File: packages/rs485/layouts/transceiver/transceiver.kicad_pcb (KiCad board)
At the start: 2 copper layers, 3 parts

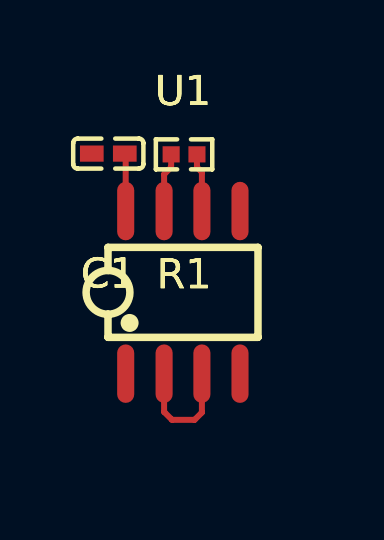
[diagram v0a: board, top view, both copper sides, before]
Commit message: Fix pulldown on RE pins
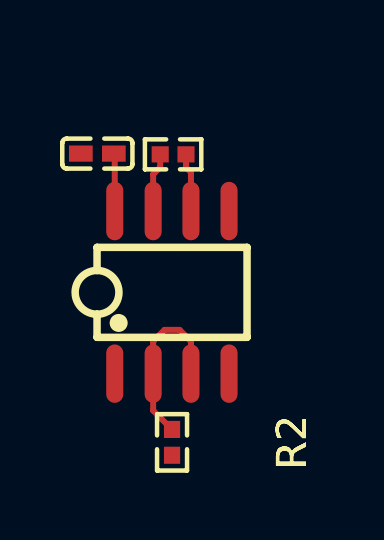
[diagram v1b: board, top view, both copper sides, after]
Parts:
- added R2: 10kΩ ±1% 62.5mW, atopile:R0402-56259e, F.Cu at (0.00, 5.00)
- moved R1 0.36 mm to (0.04, -4.60)
- moved U1 0.36 mm to (0.00, 0.00)
- moved C1 0.36 mm to (-2.49, -4.62)
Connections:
- R1 pad 1: line-1 -> line-4
- U1 pad 1: line-4 -> line
- U1 pad 2: line -> line-1
- U1 pad 3: line -> line-1
- U1 pad 6: line-1 -> line-4
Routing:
- net line: track 4.04 -> 0.00 mm
- net line-1: track 1.96 -> 5.86 mm
- net line-4: track 0.00 -> 1.96 mm

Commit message: Build all packages without designators on silkscreen.
Also disable fail_on_drc and enable keep_picked_parts for build
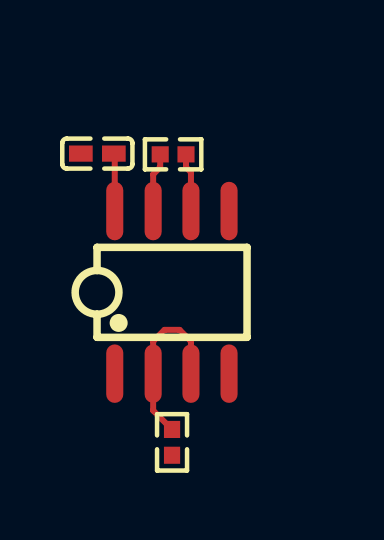
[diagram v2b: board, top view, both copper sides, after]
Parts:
- R1: value 121Ω ±1% 62.5mW -> 120Ω ±1% 62.5mW
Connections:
- R1 pad 1: line-4 -> line-2
- R1 pad 2: line-2 -> line-3
- R2 pad 1: line-1 -> line-4
- U1 pad 1: line -> line-1
- U1 pad 2: line-1 -> line-4
- U1 pad 3: line-1 -> line-4
- U1 pad 4: line-3 -> line
- U1 pad 6: line-4 -> line-2
- U1 pad 7: line-2 -> line-3
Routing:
- net line-1: track 5.86 -> 0.00 mm
- net line-4: track 1.96 -> 5.86 mm
- net line-3: track 0.00 -> 1.99 mm
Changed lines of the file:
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@@
     )
     (net 0 "")
-    (net 1 "line-2")
-    (net 2 "line")
-    (net 3 "line-3")
-    (net 4 "line-4")
+    (net 1 "line-3")
+    (net 2 "line-1")
+    (net 3 "line")
+    (net 4 "line-2")
     (net 5 "hv")
     (net 6 "gnd")
-    (net 7 "line-1")
+    (net 7 "line-4")
     (footprint "atopile:SOIC-8_L5.0-W4.0-P1.27-LS6.0-BL-294f77"
         (layer "F.Cu")
@@
             (size 0.57 1.95)
             (layers "F.Cu" "F.Mask" "F.Paste")
-            (net 2 "line")
+            (net 2 "line-1")
         )
         (pad "2" smd oval
@@
             (size 0.57 1.95)
             (layers "F.Cu" "F.Mask" "F.Paste")
-            (net 7 "line-1")
+            (net 7 "line-4")
         )
         (pad "3" smd oval
@@
             (size 0.57 1.95)
             (layers "F.Cu" "F.Mask" "F.Paste")
-            (net 7 "line-1")
+            (net 7 "line-4")
         )
         (pad "4" smd oval
@@
             (size 0.57 1.95)
             (layers "F.Cu" "F.Mask" "F.Paste")
-            (net 3 "line-3")
+            (net 3 "line")
         )
         (pad "5" smd oval
@@
             (size 0.57 1.95)
             (layers "F.Cu" "F.Mask" "F.Paste")
-            (net 4 "line-4")
+            (net 4 "line-2")
         )
         (pad "7" smd oval
@@
             (size 0.57 1.95)
             (layers "F.Cu" "F.Mask" "F.Paste")
-            (net 1 "line-2")
+            (net 1 "line-3")
         )
         (pad "8" smd oval
@@
             (at 0 -4 90)
             (layer "F.SilkS")
-            (hide no)
+            (hide yes)
             (effects
                 (font
@@
                     (thickness 0.15)
                 )
+                (hide yes)
             )
             (unlocked no)
@@
                     (thickness 0.15)
                 )
+                (hide yes)
             )
             (unlocked no)
@@
             (size 0.57 0.54)
             (layers "F.Cu" "F.Mask" "F.Paste")
-            (net 7 "line-1")
+            (net 7 "line-4")
         )
         (pad "2" smd rect
@@
             )
         )
-        (property "Value" "121Ω ±1% 62.5mW"
+        (property "Value" "120Ω ±1% 62.5mW"
             (at 0 4 0)
             (layer "F.Fab")
@@
             )
         )
-        (property "LCSC" "C25080"
-            (at 0 0 0)
-            (layer "User.9")
-            (hide yes)
-            (effects
-                (font
-                    (size 0.125 0.125)
-                    (thickness 0.01875)
-                )
-            )
-        )
-        (property "Partnumber" "0402WGF1210TCE"
-            (at 0 0 0)
-            (layer "User.9")
-            (hide yes)
-            (effects
-                (font
-                    (size 0.125 0.125)
-                    (thickness 0.01875)
-                )
-            )
-        )
-        (property "Manufacturer" "UNI-ROYAL(Uniroyal Elec)"
-            (at 0 0 0)
-            (layer "User.9")
-            (hide yes)
-            (effects
-                (font
-                    (size 0.125 0.125)
-                    (thickness 0.01875)
-                )
-            )
-        )
-        (property "JLCPCB description" "62.5mW Thick Film Resistors 50V ±100ppm/℃ ±1% 121Ω 0402 Chip Resistor - Surface Mount ROHS"
+        (property "LCSC" "C114758"
+            (at 0 0 0)
+            (layer "User.9")
+            (hide yes)
+            (effects
+                (font
+                    (size 0.125 0.125)
+                    (thickness 0.01875)
+                )
+            )
+        )
+        (property "Partnumber" "RC0402FR-07120RL"
+            (at 0 0 0)
+            (layer "User.9")
+            (hide yes)
+            (effects
+                (font
+                    (size 0.125 0.125)
+                    (thickness 0.01875)
+                )
+            )
+        )
+        (property "Manufacturer" "YAGEO"
+            (at 0 0 0)
+            (layer "User.9")
+            (hide yes)
+            (effects
+                (font
+                    (size 0.125 0.125)
+                    (thickness 0.01875)
+                )
+            )
+        )
+        (property "JLCPCB description" "62.5mW Thick Film Resistors 50V ±100ppm/℃ ±1% 120Ω 0402 Chip Resistor - Surface Mount ROHS"
             (at 0 0 0)
             (layer "User.9")
@@
             )
         )
-        (property "PARAM_resistance" "{\"type\": \"Quantity_Interval_Disjoint\", \"data\": {\"intervals\": {\"type\": \"Numeric_Interval_Disjoint\", \"data\": {\"intervals\": [{\"type\": \"Numeric_Interval\", \"data\": {\"min\": 119.79000002704561, \"max\": 122.20999997295439}}]}}, \"unit\": \"ohm\"}}"
+        (property "PARAM_resistance" "{\"type\": \"Quantity_Interval_Disjoint\", \"data\": {\"intervals\": {\"type\": \"Numeric_Interval_Disjoint\", \"data\": {\"intervals\": [{\"type\": \"Numeric_Interval\", \"data\": {\"min\": 118.80000002682209, \"max\": 121.19999997317791}}]}}, \"unit\": \"ohm\"}}"
             (at 0 0 0)
             (layer "User.9")
@@
             (size 0.57 0.54)
             (layers "F.Cu" "F.Mask" "F.Paste")
-            (net 4 "line-4")
+            (net 4 "line-2")
         )
         (pad "2" smd rect
@@
             (size 0.57 0.54)
             (layers "F.Cu" "F.Mask" "F.Paste")
-            (net 1 "line-2")
+            (net 1 "line-3")
         )
         (embedded_fonts no)

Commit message: Fix publish on failed build & fix pull resistor that should not be there (#2)
* Remove pull resistor (should not be part of the tranceiver)

* Fix publish if build fails
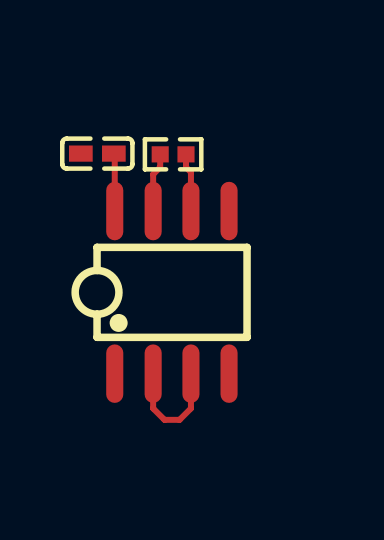
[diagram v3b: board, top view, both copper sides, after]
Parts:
- removed R2: 10kΩ ±1% 62.5mW, atopile:R0402-56259e
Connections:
- R1 pad 2: line-3 -> line-4
- U1 pad 1: line-1 -> line-3
- U1 pad 2: line-4 -> line-1
- U1 pad 3: line-4 -> line-1
- U1 pad 7: line-3 -> line-4
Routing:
- net line-1: track 0.00 -> 3.89 mm
- net line-4: track 5.86 -> 1.99 mm
- net line-3: track 1.99 -> 0.00 mm

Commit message: Rebuild rs485 package
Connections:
- R1 pad 2: line-4 -> line-3
- U1 pad 1: line-3 -> line-1
- U1 pad 2: line-1 -> line-4
- U1 pad 3: line-1 -> line-4
- U1 pad 7: line-4 -> line-3
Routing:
- net line-1: track 3.89 -> 0.00 mm
- net line-3: track 0.00 -> 1.99 mm
- net line-4: track 1.99 -> 3.89 mm
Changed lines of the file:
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@@
     )
     (net 0 "")
-    (net 1 "line-4")
-    (net 2 "line-3")
+    (net 1 "line-3")
+    (net 2 "line-1")
     (net 3 "line")
     (net 4 "line-2")
     (net 5 "hv")
     (net 6 "gnd")
-    (net 7 "line-1")
+    (net 7 "line-4")
     (footprint "atopile:SOIC-8_L5.0-W4.0-P1.27-LS6.0-BL-294f77"
         (layer "F.Cu")
@@
             (size 0.57 1.95)
             (layers "F.Cu" "F.Mask" "F.Paste")
-            (net 2 "line-3")
+            (net 2 "line-1")
         )
         (pad "2" smd oval
@@
             (size 0.57 1.95)
             (layers "F.Cu" "F.Mask" "F.Paste")
-            (net 7 "line-1")
+            (net 7 "line-4")
         )
         (pad "3" smd oval
@@
             (size 0.57 1.95)
             (layers "F.Cu" "F.Mask" "F.Paste")
-            (net 7 "line-1")
+            (net 7 "line-4")
         )
         (pad "4" smd oval
@@
             (size 0.57 1.95)
             (layers "F.Cu" "F.Mask" "F.Paste")
-            (net 1 "line-4")
+            (net 1 "line-3")
         )
         (pad "8" smd oval
@@
             (size 0.57 0.54)
             (layers "F.Cu" "F.Mask" "F.Paste")
-            (net 1 "line-4")
+            (net 1 "line-3")
         )
         (embedded_fonts no)
